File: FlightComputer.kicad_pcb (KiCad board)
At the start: 6 copper layers, 60 x 60 mm, 79 parts, among them J1 Conn_01x05_Pin, J10 503182-1852, J2 Conn_01x03_Pin, J3 Conn_01x06_Pin, J4 Conn_01x03_Pin, J5 Conn_01x03, J6 Conn_01x03, J7 Screw_Terminal_01x02, J8 Screw_Terminal_01x02, J9 Conn_ST_STDC14, Q1 2N7002, Q2 2N7002, Q3 IRFR9120N, Q4 IRFR9120N, U1 BMM350, U2 INA260, U3 BMP581, U5 ICM-45686, U6 STM32F722RETx, U7 STM32H757XIHx, Y1 25MHz, Y2 32.768kHz

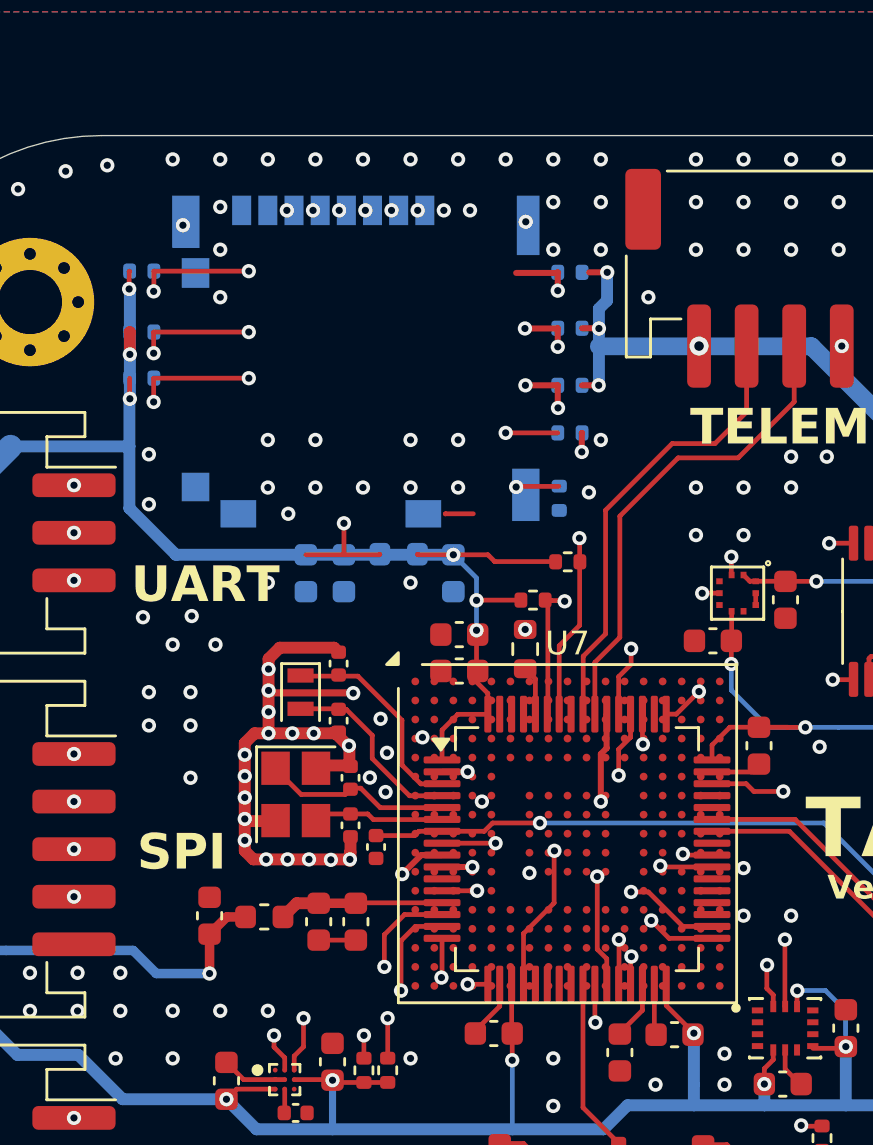
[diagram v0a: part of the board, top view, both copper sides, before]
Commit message: Added GPS
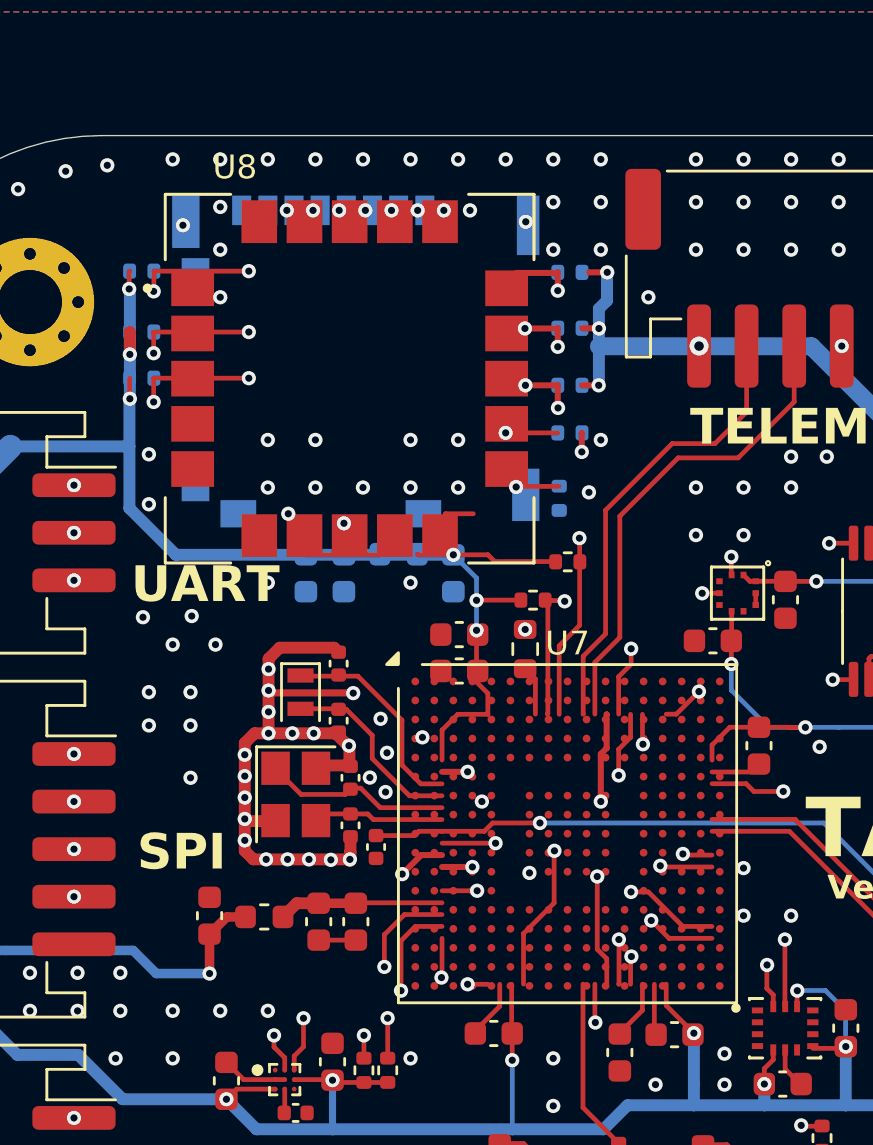
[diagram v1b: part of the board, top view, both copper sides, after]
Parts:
- removed U6: STM32F722RETx, Package_QFP:LQFP-64_10x10mm_P0.5mm
- added U8: SAM-M10Q-00B, SAM-M10Q-00B:XCVR_SAM-M10Q-00B, F.Cu at (215.4, 70.2)
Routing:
- net GND: vias 262 -> 261
- net /SDMMC1_D2: vias 4 -> 5

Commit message: added files for the schematic
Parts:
- removed C10, C14, C16, C17, C18, C20, C21: 100nF, Capacitor_SMD:C_0603_1608Metric
- removed C15: 100nF, Capacitor_SMD:C_0402_1005Metric
- removed C19: 4.7uF, Capacitor_SMD:C_0603_1608Metric
- removed C22: 10nF, Capacitor_SMD:C_0603_1608Metric
- removed C23, C24: 1uF, Capacitor_SMD:C_0603_1608Metric
- removed FB1: 100R, Inductor_SMD:L_0603_1608Metric
- removed R1: 100k, Resistor_SMD:R_0603_1608Metric
- removed R15, R16: 4.7k, Resistor_SMD:R_0402_1005Metric
- removed U5: ICM-45686, ICM-45686:IC_ICM-45686
- added C28: 100nF, Capacitor_SMD:C_0603_1608Metric, F.Cu at (157.7, 77.0)
- added C29: 100nF, Capacitor_SMD:C_0603_1608Metric, F.Cu at (157.7, 79.5)
- added C30: 100nF, Capacitor_SMD:C_0603_1608Metric, F.Cu at (157.7, 82.1)
- added C31: 100nF, Capacitor_SMD:C_0603_1608Metric, F.Cu at (157.7, 84.6)
- added C32: 100nF, Capacitor_SMD:C_0603_1608Metric, F.Cu at (161.8, 67.0)
- added C33: 100nF, Capacitor_SMD:C_0603_1608Metric, F.Cu at (161.8, 69.5)
- added C34: 100nF, Capacitor_SMD:C_0603_1608Metric, F.Cu at (161.8, 72.0)
- added C35: 100nF, Capacitor_SMD:C_0603_1608Metric, F.Cu at (161.8, 74.5)
- added C36: 100nF, Capacitor_SMD:C_0603_1608Metric, F.Cu at (161.8, 77.0)
- added C37: 100nF, Capacitor_SMD:C_0603_1608Metric, F.Cu at (161.8, 79.5)
- added C38: 100nF, Capacitor_SMD:C_0603_1608Metric, F.Cu at (161.8, 82.1)
- added C39: 100nF, Capacitor_SMD:C_0603_1608Metric, F.Cu at (161.8, 84.6)
- added C40: 100nF, Capacitor_SMD:C_0603_1608Metric, F.Cu at (165.8, 67.0)
- added C41: 100nF, Capacitor_SMD:C_0603_1608Metric, F.Cu at (165.8, 69.5)
- added C42: 100nF, Capacitor_SMD:C_0603_1608Metric, F.Cu at (165.8, 72.0)
- added C43: 100nF, Capacitor_SMD:C_0603_1608Metric, F.Cu at (165.8, 74.5)
- added C44: 100nF, Capacitor_SMD:C_0603_1608Metric, F.Cu at (165.8, 77.0)
- added C45: 100nF, Capacitor_SMD:C_0603_1608Metric, F.Cu at (165.8, 79.5)
- added C46: 100nF, Capacitor_SMD:C_0603_1608Metric, F.Cu at (165.8, 82.1)
- added C47: 100nF, Capacitor_SMD:C_0603_1608Metric, F.Cu at (165.8, 84.6)
- added C48: 100nF, Capacitor_SMD:C_0603_1608Metric, F.Cu at (169.8, 67.0)
- added C49: 100nF, Capacitor_SMD:C_0402_1005Metric, F.Cu at (188.1, 80.7)
- added C50: 100nF, Capacitor_SMD:C_0603_1608Metric, F.Cu at (169.8, 69.5)
- added C51: 100nF, Capacitor_SMD:C_0603_1608Metric, F.Cu at (169.8, 72.0)
- added C52: 10uF, Capacitor_SMD:C_0603_1608Metric, F.Cu at (169.8, 74.5)
- added C53: 4.7uF, Capacitor_SMD:C_0603_1608Metric, F.Cu at (169.8, 77.0)
- added C54: 4.7uF, Capacitor_SMD:C_0603_1608Metric, F.Cu at (169.8, 79.5)
- added C55: 4.7uF, Capacitor_SMD:C_0603_1608Metric, F.Cu at (169.8, 82.1)
- added C56: 100nF, Capacitor_SMD:C_0603_1608Metric, F.Cu at (169.8, 84.6)
- added C57: 100nF, Capacitor_SMD:C_0603_1608Metric, F.Cu at (173.8, 67.0)
- added C58: 10uF, Capacitor_SMD:C_0603_1608Metric, F.Cu at (173.8, 69.5)
- added C59: 10uF, Capacitor_SMD:C_0603_1608Metric, F.Cu at (173.8, 72.0)
- added C60: 2.2uF, Capacitor_SMD:C_0603_1608Metric, F.Cu at (173.8, 74.5)
- added C61: 2.2uF, Capacitor_SMD:C_0603_1608Metric, F.Cu at (173.8, 77.0)
- added C63: 10nF, Capacitor_SMD:C_0603_1608Metric, F.Cu at (173.8, 79.5)
- added C64: 1uF, Capacitor_SMD:C_0603_1608Metric, F.Cu at (173.8, 82.1)
- added C65: 1uF, Capacitor_SMD:C_0603_1608Metric, F.Cu at (173.8, 84.6)
- added C66: 220pF, Capacitor_SMD:C_0603_1608Metric, F.Cu at (177.8, 67.0)
- added FB3: 100R, Inductor_SMD:L_0603_1608Metric, F.Cu at (177.8, 72.0)
- added R23: 100k, Resistor_SMD:R_0603_1608Metric, F.Cu at (177.8, 74.5)
- added R24: 4.7k, Resistor_SMD:R_0603_1608Metric, F.Cu at (177.8, 77.0)
- added R25: 4.7k, Resistor_SMD:R_0603_1608Metric, F.Cu at (177.8, 79.5)
- added R26: 10k, Resistor_SMD:R_0603_1608Metric, F.Cu at (177.8, 82.1)
- added R27: 10k, Resistor_SMD:R_0603_1608Metric, F.Cu at (177.8, 84.6)
- C25, C26, C27, FB2, J10, R12, R13, R14, R17, R18, R19, R21, R22: moved to F.Cu
- moved C1 74.3 mm to (157.7, 67.0), turned to 0 degrees
- moved C27 62.2 mm to (157.7, 74.5), turned to 0 degrees
- moved R19 59.2 mm to (174.2, 96.8)
- moved R22 58.8 mm to (174.2, 100.8)
- moved C26 57.8 mm to (157.7, 72.0), turned to 0 degrees
- moved J10 57.3 mm to (164.3, 94.8), turned to 0 degrees
- moved R21 56.9 mm to (174.2, 98.8)
- moved C25 56.6 mm to (157.7, 69.5), turned to 0 degrees
- moved R14 55.3 mm to (174.2, 90.8)
- moved R17 53.0 mm to (174.2, 92.8), turned to 0 degrees
- moved R18 41.9 mm to (174.2, 94.8), turned to 0 degrees
- moved FB2 40.5 mm to (177.8, 69.5), turned to 0 degrees
- moved R12 38.7 mm to (174.2, 86.8), turned to 0 degrees
- moved R13 37.4 mm to (174.2, 88.8), turned to 0 degrees
- moved Y2 36.8 mm to (177.5, 91.7), turned to 0 degrees
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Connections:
- J9 pad 13: /UART1_TX -> unconnected-(J9-VCP_RX-Pad13)
- J9 pad 14: /UART1_RX -> unconnected-(J9-VCP_TX-Pad14)
- U1 pad A2: IMU_SDA -> I2C3_SDA
- U1 pad A3: IMU_SCL -> I2C3_SCL
- U4 pad 13: IMU_SCL -> I2C3_SCL
- U4 pad 14: IMU_SDA -> I2C3_SDA
- U7 pad A1: Net-(U7-VSS-PadA1) -> GND
- U7 pad A13: unconnected-(U7-PC10-PadA13) -> /SDMMC1_D2
- U7 pad A17: Net-(U7-VSS-PadA1) -> GND
- U7 pad A6: unconnected-(U7-VDDLDO-PadA6) -> 3V3
- U7 pad A7: unconnected-(U7-VCAP-PadA7) -> Net-(C60-Pad1)
- U7 pad B1: unconnected-(U7-VBAT-PadB1) -> 3V3
- U7 pad B13: unconnected-(U7-PC11-PadB13) -> /SDMMC1_D3
- U7 pad B14: unconnected-(U7-PA14-PadB14) -> /SWCLK
- U7 pad B2: Net-(U7-VSS-PadA1) -> GND
- U7 pad B5: unconnected-(U7-PB6-PadB5) -> SCL1
- U7 pad B6: Net-(U7-VSS-PadA1) -> GND
- U7 pad C1: unconnected-(U7-PC15-PadC1) -> /LSE_OUT
- U7 pad C10: Net-(U7-VSS-PadA1) -> GND
- U7 pad C12: unconnected-(U7-PC12-PadC12) -> /SDMMC1_CLK
- U7 pad C13: Net-(U7-VSS-PadA1) -> GND
- U7 pad C15: unconnected-(U7-PA13-PadC15) -> /SWDIO
- U7 pad C16: Net-(U7-VSS-PadA1) -> GND
- U7 pad C17: unconnected-(U7-VDDLDO-PadC17) -> 3V3
- U7 pad C2: unconnected-(U7-PC14-PadC2) -> /LSE_IN
- U7 pad C5: unconnected-(U7-PB7-PadC5) -> SDA1
- U7 pad D12: unconnected-(U7-PD2-PadD12) -> /SDMMC1_CMD
- U7 pad D17: unconnected-(U7-VCAP-PadD17) -> Net-(C61-Pad1)
- U7 pad E1: unconnected-(U7-VLXSMPS-PadE1) -> Net-(U7-VLXSMPS)
- U7 pad E11: unconnected-(U7-VDD-PadE11) -> 3V3
- U7 pad E13: unconnected-(U7-PC8-PadE13) -> /SDMMC1_D0
- U7 pad E14: unconnected-(U7-PC9-PadE14) -> /SDMMC1_D1
- U7 pad E6: unconnected-(U7-VDD-PadE6) -> 3V3
- U7 pad E7: unconnected-(U7-PDR_ON-PadE7) -> 3V3
- U7 pad E8: unconnected-(U7-BOOT0-PadE8) -> Net-(U7-BOOT0)
- U7 pad E9: unconnected-(U7-VDD-PadE9) -> 3V3
- U7 pad F1: unconnected-(U7-VDDSMPS-PadF1) -> 3V3
- U7 pad F17: unconnected-(U7-VDD33_USB-PadF17) -> 3V3
- U7 pad F2: unconnected-(U7-VSSSMPS-PadF2) -> GND
- U7 pad F5: unconnected-(U7-VDD-PadF5) -> 3V3
- U7 pad G10: Net-(U7-VSS-PadA1) -> GND
- U7 pad G11: Net-(U7-VSS-PadA1) -> GND
- U7 pad G13: unconnected-(U7-VDD-PadG13) -> 3V3
- U7 pad G16: Net-(U7-VSS-PadA1) -> GND
- U7 pad G17: unconnected-(U7-VDD50_USB-PadG17) -> 3V3
- U7 pad G2: unconnected-(U7-VFBSMPS-PadG2) -> Net-(U7-VFBSMPS)
- U7 pad G5: unconnected-(U7-VDD-PadG5) -> 3V3
- U7 pad G7: Net-(U7-VSS-PadA1) -> GND
- U7 pad G8: Net-(U7-VSS-PadA1) -> GND
- U7 pad G9: Net-(U7-VSS-PadA1) -> GND
- U7 pad H10: Net-(U7-VSS-PadA1) -> GND
- U7 pad H11: Net-(U7-VSS-PadA1) -> GND
- U7 pad H13: unconnected-(U7-VDD-PadH13) -> 3V3
- U7 pad H5: unconnected-(U7-VDD-PadH5) -> 3V3
- U7 pad H7: Net-(U7-VSS-PadA1) -> GND
- U7 pad H8: Net-(U7-VSS-PadA1) -> GND
- U7 pad H9: Net-(U7-VSS-PadA1) -> GND
- U7 pad J1: unconnected-(U7-PH1-PadJ1) -> /HSE_OUT
- U7 pad J10: Net-(U7-VSS-PadA1) -> GND
- U7 pad J11: Net-(U7-VSS-PadA1) -> GND
- U7 pad J13: unconnected-(U7-VDD-PadJ13) -> 3V3
- U7 pad J16: Net-(U7-VSS-PadA1) -> GND
- U7 pad J17: Net-(U7-VSS-PadA1) -> GND
- U7 pad J2: unconnected-(U7-PH0-PadJ2) -> /HSE_IN
- U7 pad J3: Net-(U7-VSS-PadA1) -> GND
- U7 pad J7: Net-(U7-VSS-PadA1) -> GND
- U7 pad J8: Net-(U7-VSS-PadA1) -> GND
- U7 pad J9: Net-(U7-VSS-PadA1) -> GND
- U7 pad K1: unconnected-(U7-NRST-PadK1) -> /~{NRST}
- U7 pad K10: Net-(U7-VSS-PadA1) -> GND
- U7 pad K11: Net-(U7-VSS-PadA1) -> GND
- U7 pad K13: unconnected-(U7-VDD-PadK13) -> 3V3
- U7 pad K15: Net-(U7-VSSDSI-PadK15) -> GND
- U7 pad K5: unconnected-(U7-VDD-PadK5) -> 3V3
- U7 pad K7: Net-(U7-VSS-PadA1) -> GND
- U7 pad K8: Net-(U7-VSS-PadA1) -> GND
- U7 pad K9: Net-(U7-VSS-PadA1) -> GND
- U7 pad L1: unconnected-(U7-VDDA-PadL1) -> VREF
- U7 pad L10: Net-(U7-VSS-PadA1) -> GND
- U7 pad L11: Net-(U7-VSS-PadA1) -> GND
- U7 pad L13: unconnected-(U7-VDD-PadL13) -> 3V3
- U7 pad L15: Net-(U7-VSSDSI-PadK15) -> GND
- U7 pad L5: unconnected-(U7-VDD-PadL5) -> 3V3
- U7 pad L7: Net-(U7-VSS-PadA1) -> GND
- U7 pad L8: Net-(U7-VSS-PadA1) -> GND
- U7 pad L9: Net-(U7-VSS-PadA1) -> GND
- U7 pad M1: unconnected-(U7-VREF+-PadM1) -> VREF
- U7 pad M13: unconnected-(U7-VDD-PadM13) -> 3V3
- U7 pad M15: Net-(U7-VSSDSI-PadK15) -> GND
- U7 pad M5: unconnected-(U7-VDD-PadM5) -> 3V3
- U7 pad N1: unconnected-(U7-VREF--PadN1) -> GND
- U7 pad N10: unconnected-(U7-VDD-PadN10) -> 3V3
- U7 pad N11: unconnected-(U7-VDD-PadN11) -> 3V3
- U7 pad N12: unconnected-(U7-VDD-PadN12) -> 3V3
- U7 pad N16: Net-(U7-VSS-PadA1) -> GND
- U7 pad N7: unconnected-(U7-VDD-PadN7) -> 3V3
- U7 pad N8: unconnected-(U7-VDD-PadN8) -> 3V3
- U7 pad P1: unconnected-(U7-VSSA-PadP1) -> GND
- U7 pad P17: unconnected-(U7-VDDDSI-PadP17) -> 3V3
- U7 pad R4: Net-(U7-VSS-PadA1) -> GND
- U7 pad R8: Net-(U7-VSS-PadA1) -> GND
- U7 pad T12: Net-(U7-VSS-PadA1) -> GND
- U7 pad T13: unconnected-(U7-PH8-PadT13) -> I2C3_SDA
- U7 pad U1: Net-(U7-VSS-PadA1) -> GND
- U7 pad U10: unconnected-(U7-PE14-PadU10) -> /IGNITE
- U7 pad U11: unconnected-(U7-VCAP-PadU11) -> Net-(C61-Pad1)
- U7 pad U12: unconnected-(U7-VDDLDO-PadU12) -> 3V3
- U7 pad U13: unconnected-(U7-PH7-PadU13) -> I2C3_SCL
- U7 pad U17: Net-(U7-VSS-PadA1) -> GND
- U7 pad U4: unconnected-(U7-PC5-PadU4) -> /DEPLOY
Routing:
- net 3V3: track 265.1 -> 85.6 mm, vias 26 -> 7
- net /SDMMC1_CMD: track 65.5 -> 0.00 mm, vias 6 -> 0
- net /SDMMC1_D3: track 58.7 -> 0.00 mm, vias 6 -> 0
- net /SDMMC1_D2: track 42.9 -> 0.00 mm, vias 5 -> 0
- net GND: track 62.3 -> 20.1 mm, vias 261 -> 121
- net IMU_SCL: track 39.5 -> 1.68 mm, vias 5 -> 0
- net /SDMMC1_D0: track 35.7 -> 0.00 mm, vias 4 -> 0
- net /SDMMC1_D1: track 33.9 -> 0.00 mm, vias 4 -> 0
- net /UART4_RX: track 32.6 -> 0.00 mm, vias 2 -> 0
- net /UART4_TX: track 32.1 -> 0.00 mm, vias 2 -> 0
- net /SPI2_SCK: track 29.4 -> 0.00 mm, vias 2 -> 0
- net IMU_SDA: track 35.8 -> 6.62 mm, vias 5 -> 2
- net /SDMMC1_SW: track 29.1 -> 0.00 mm, vias 2 -> 0
- net /SPI3_NSS: track 34.0 -> 5.05 mm, vias 2 -> 0
- net /SPI2_NSS: track 28.6 -> 0.00 mm, vias 2 -> 0
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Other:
- board text removed: "MISO"
- board text removed: "MOSI"
- board text removed: "NSS"
- board text removed: "RX"
- board text removed: "SCK"
- board text removed: "SPI"
- board text removed: "TELEMETRY"
- board text removed: "TX"

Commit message: updated
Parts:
- added C1: 100nF, Capacitor_SMD:C_0402_1005Metric, B.Cu at (214.7, 65.5)
- added C3: 100nF, Capacitor_SMD:C_0402_1005Metric, B.Cu at (218.1, 65.5)
- added C4: 100nF, Capacitor_SMD:C_0603_1608Metric, F.Cu at (224.1, 75.1)
- added L1: 2.2uH, Capacitor_SMD:C_1812_4532Metric, B.Cu at (216.0, 87.3)
- C19: renamed from C49; moved to B.Cu
- C20: renamed from C59; footprint Capacitor_SMD:C_0603_1608Metric -> Capacitor_SMD:C_0402_1005Metric; moved to B.Cu
- C21: renamed from C60; footprint Capacitor_SMD:C_0603_1608Metric -> Capacitor_SMD:C_0402_1005Metric
- C22: renamed from C58; footprint Capacitor_SMD:C_0603_1608Metric -> Capacitor_SMD:C_0402_1005Metric; moved to B.Cu
- C23: renamed from C66; footprint Capacitor_SMD:C_0603_1608Metric -> Capacitor_SMD:C_0402_1005Metric; moved to B.Cu
- C24: renamed from C61; footprint Capacitor_SMD:C_0603_1608Metric -> Capacitor_SMD:C_0402_1005Metric
- C27: renamed from C35; footprint Capacitor_SMD:C_0603_1608Metric -> Capacitor_SMD:C_0402_1005Metric
- C28: footprint Capacitor_SMD:C_0603_1608Metric -> Capacitor_SMD:C_0402_1005Metric; moved to B.Cu
- C31: renamed from C36; footprint Capacitor_SMD:C_0603_1608Metric -> Capacitor_SMD:C_0402_1005Metric
- C32: renamed from C29; footprint Capacitor_SMD:C_0603_1608Metric -> Capacitor_SMD:C_0402_1005Metric; moved to B.Cu
- C35: renamed from C37; footprint Capacitor_SMD:C_0603_1608Metric -> Capacitor_SMD:C_0402_1005Metric
- C36: renamed from C30; footprint Capacitor_SMD:C_0603_1608Metric -> Capacitor_SMD:C_0402_1005Metric; moved to B.Cu
- C39: renamed from C38; footprint Capacitor_SMD:C_0603_1608Metric -> Capacitor_SMD:C_0402_1005Metric
- C40: renamed from C31; footprint Capacitor_SMD:C_0603_1608Metric -> Capacitor_SMD:C_0402_1005Metric; moved to B.Cu
- C43: renamed from C39; footprint Capacitor_SMD:C_0603_1608Metric -> Capacitor_SMD:C_0402_1005Metric
- C44: renamed from C32; footprint Capacitor_SMD:C_0603_1608Metric -> Capacitor_SMD:C_0402_1005Metric; moved to B.Cu
- C47: renamed from C40; footprint Capacitor_SMD:C_0603_1608Metric -> Capacitor_SMD:C_0402_1005Metric
- C48: renamed from C33; footprint Capacitor_SMD:C_0603_1608Metric -> Capacitor_SMD:C_0402_1005Metric; moved to B.Cu
- C51: renamed from C41; footprint Capacitor_SMD:C_0603_1608Metric -> Capacitor_SMD:C_0402_1005Metric; moved to B.Cu
- C52: renamed from C34; footprint Capacitor_SMD:C_0603_1608Metric -> Capacitor_SMD:C_0402_1005Metric; moved to B.Cu
- C53: renamed from C52; value 10uF -> 4.7uF; footprint Capacitor_SMD:C_0603_1608Metric -> Capacitor_SMD:C_0402_1005Metric; moved to B.Cu
- J10: moved to B.Cu
- J5: renamed from J3; footprint Connector_JST:JST_PH_S6B-PH-SM4-TB_1x06-1MP_P2.00mm_Horizontal -> Connector_JST:JST_PH_S8B-PH-SM4-TB_1x08-1MP_P2.00mm_Horizontal
- R5: renamed from R17; moved to B.Cu
- moved C36 76.0 mm to (233.6, 87.0), turned to 90 degrees
- moved C40 75.9 mm to (233.6, 88.9), turned to -90 degrees
- moved J10 74.5 mm to (234.2, 69.2), turned to 180 degrees
- moved C44 74.1 mm to (233.8, 84.5), turned to 90 degrees
- moved C32 72.7 mm to (227.9, 98.5), turned to 180 degrees
- moved C48 62.1 mm to (221.0, 88.1), turned to -90 degrees
- moved C52 61.7 mm to (220.8, 89.9), turned to -90 degrees
- moved C28 60.1 mm to (217.5, 83.3), turned to 90 degrees
- moved C47 58.7 mm to (223.2, 79.1)
- moved C51 57.9 mm to (222.1, 82.7), turned to 180 degrees
- moved R5 56.0 mm to (227.9, 77.0)
- moved C21 50.0 mm to (223.4, 81.0), turned to 90 degrees
- moved C54 45.1 mm to (216.1, 95.1), turned to -90 degrees
- moved C23 44.2 mm to (217.4, 86.4), turned to -90 degrees
- moved C20 43.2 mm to (214.7, 85.9), turned to 90 degrees
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- renumbered C9 to C10, C2 to C11, C11 to C12, C5 to C13, C12 to C14, C6 to C15, C25 to C16, C26 to C17, C27 to C18, C7 to C2, C50 to C25, C42 to C26, C51 to C29, C43 to C30, C53 to C33, C44 to C34, C54 to C37, C45 to C38, C55 to C41, C46 to C42, C56 to C45, C47 to C46, C57 to C49, C4 to C5, C48 to C50, C63 to C54, C64 to C55, C65 to C56, C13 to C6, C3 to C7, C1 to C8, C8 to C9, FB2 to FB1, FB3 to FB2, J5 to J3, J6 to J4, J4 to J6, J9 to J7, J7 to J8, J8 to J9, R20 to R1, R4 to R10, R5 to R11, R6 to R12, R7 to R13, R8 to R14, R9 to R15, R21 to R16, R22 to R17, R23 to R18, R27 to R19, R12 to R2, R26 to R20, R24 to R21, R25 to R22, R13 to R3, R14 to R4, R18 to R6, R19 to R7, R2 to R8, R3 to R9, U4 to U1, U8 to U3, U1 to U4, U3 to U5, U7 to U6
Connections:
- J2 pad 1: /UART2_TX -> /UART4_TX
- J2 pad 2: /UART2_RX -> /UART4_RX
- J6 pad 1: /UART4_TX -> unconnected-(J6-Pin_1-Pad1)
- J6 pad 2: /UART4_RX -> unconnected-(J6-Pin_2-Pad2)
- U1 pad 4: unconnected-(U4-INT1-Pad4) -> LSM_INT1
- U1 pad 9: unconnected-(U4-INT2-Pad9) -> LSM_INT2
- U2 pad 7: unconnected-(U2-ALERT-Pad7) -> INA260_INT
- U3 pad 1: Net-(U8-GND-Pad1) -> GND
- U3 pad 10: Net-(U8-GND-Pad1) -> GND
- U3 pad 11: Net-(U8-GND-Pad1) -> GND
- U3 pad 13: unconnected-(U8-TXD-Pad13) -> GNSS_RX
- U3 pad 14: unconnected-(U8-RXD-Pad14) -> GNSS_TX
- U3 pad 15: Net-(U8-GND-Pad1) -> GND
- U3 pad 16: Net-(U8-GND-Pad1) -> GND
- U3 pad 17: unconnected-(U8-VCC-Pad17) -> Net-(U3-VCC)
- U3 pad 18: unconnected-(U8-~{RESET}-Pad18) -> GNSS_RST
- U3 pad 2: unconnected-(U8-V_IO-Pad2) -> Net-(U3-VCC)
- U3 pad 20: Net-(U8-GND-Pad1) -> GND
- U3 pad 3: unconnected-(U8-V_BCKP-Pad3) -> Net-(U3-VCC)
- U3 pad 4: Net-(U8-GND-Pad1) -> GND
- U3 pad 5: Net-(U8-GND-Pad1) -> GND
- U3 pad 6: Net-(U8-GND-Pad1) -> GND
- U4 pad A1: unconnected-(U1-INT-PadA1) -> BMM350_INT
- U5 pad 7: unconnected-(U3-INT-Pad7) -> BMP581_INT
- U6 pad B14: /SWCLK -> /SWDCLK
- U6 pad B4: unconnected-(U7-PE1-PadB4) -> GNSS_TX
- U6 pad C4: unconnected-(U7-PE0-PadC4) -> GNSS_RX
- U6 pad T1: unconnected-(U7-PA0_C-PadT1) -> /UART4_TX
- U6 pad T2: unconnected-(U7-PA1_C-PadT2) -> /UART4_RX
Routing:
- net 3V3: track 85.6 -> 1.51 mm, vias 7 -> 0
- net +24V: track 32.8 -> 0.00 mm, vias 3 -> 0
- net Net-(D1-K): track 19.9 -> 0.00 mm
- net /PWR_PAD: track 18.5 -> 0.00 mm
- net /SWDIO: track 17.1 -> 0.00 mm, vias 1 -> 0
- net /~{NRST}: track 16.6 -> 1.26 mm
- net unconnected-(J7-VCP_TX-Pad14): track 13.1 -> 0.00 mm, vias 2 -> 0
- net SCL1: track 12.3 -> 0.52 mm, vias 2 -> 1
- net /SWDCLK: track 11.3 -> 0.00 mm, vias 1 -> 0
- net GNSS_RX: track 0.00 -> 10.7 mm, vias 0 -> 2
- net /DEPLOY: track 10.1 -> 0.00 mm, vias 1 -> 0
- net SDA1: track 9.97 -> 0.55 mm, vias 2 -> 1
- net unconnected-(J7-VCP_RX-Pad13): track 9.31 -> 0.00 mm
- net GNSS_TX: track 0.00 -> 9.11 mm, vias 0 -> 2
- net VREF: track 0.00 -> 7.10 mm
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- removed copper zone on F.Cu, net /3V3_EXT
- removed copper zone on B.Cu, net 3V3
- removed copper zone on F.Cu, net 3V3
- removed copper zone on In1.Cu, net 3V3
- removed copper zone on In2.Cu, net 3V3
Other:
- board text added: "Version 2"
- board text removed: "Version 1"
